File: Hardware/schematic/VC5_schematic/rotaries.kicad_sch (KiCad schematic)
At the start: 39 parts, among them U6 MCP23017

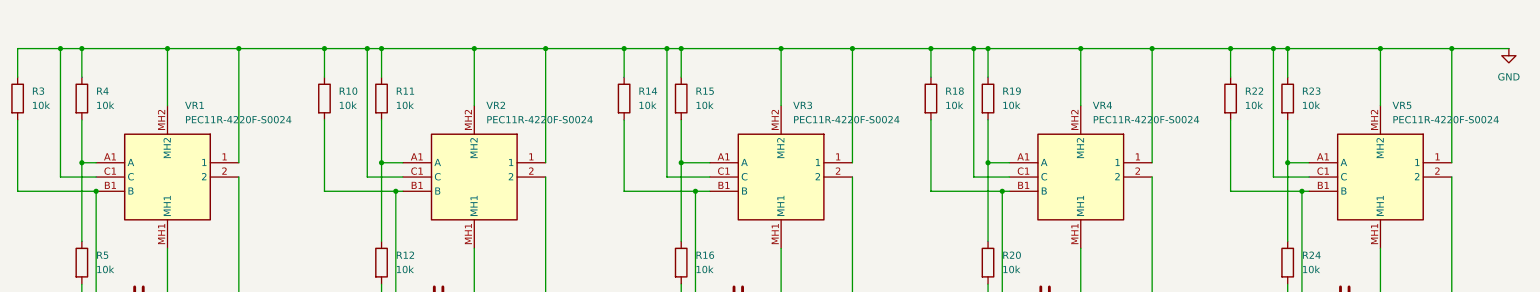
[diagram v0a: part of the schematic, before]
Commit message: fixed an error in the filters for the rotaries
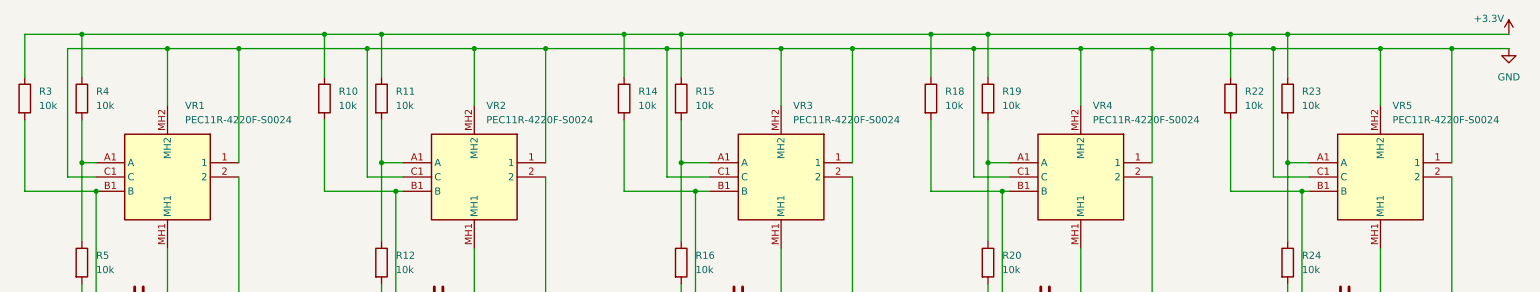
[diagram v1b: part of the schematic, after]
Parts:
- C10, C11, C12, C13, C14, C15, C6, C7, C8, C9: footprint (none) -> Capacitor_THT:C_Disc_D3.8mm_W2.6mm_P2.50mm
- R10, R11, R12, R13, R14, R15, R16, R17, R18, R19, R20, R21, R22, R23, R24, R25, R3, R4, R5, R6: footprint (none) -> Resistor_THT:R_Axial_DIN0204_L3.6mm_D1.6mm_P7.62mm_Horizontal
- R7, R8, R9: footprint Resistor_THT:R_Axial_DIN0207_L6.3mm_D2.5mm_P10.16mm_Horizontal -> Resistor_THT:R_Axial_DIN0204_L3.6mm_D1.6mm_P7.62mm_Horizontal
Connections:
- net +3.3V: now also R10.1, R11.1, R14.1, R15.1, R18.1, R19.1, R22.1, R23.1, R3.1, R4.1
- net GND: no longer R10.1, R11.1, R14.1, R15.1, R18.1, R19.1, R22.1, R23.1, R3.1, R4.1
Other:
- moved on the sheet: R3

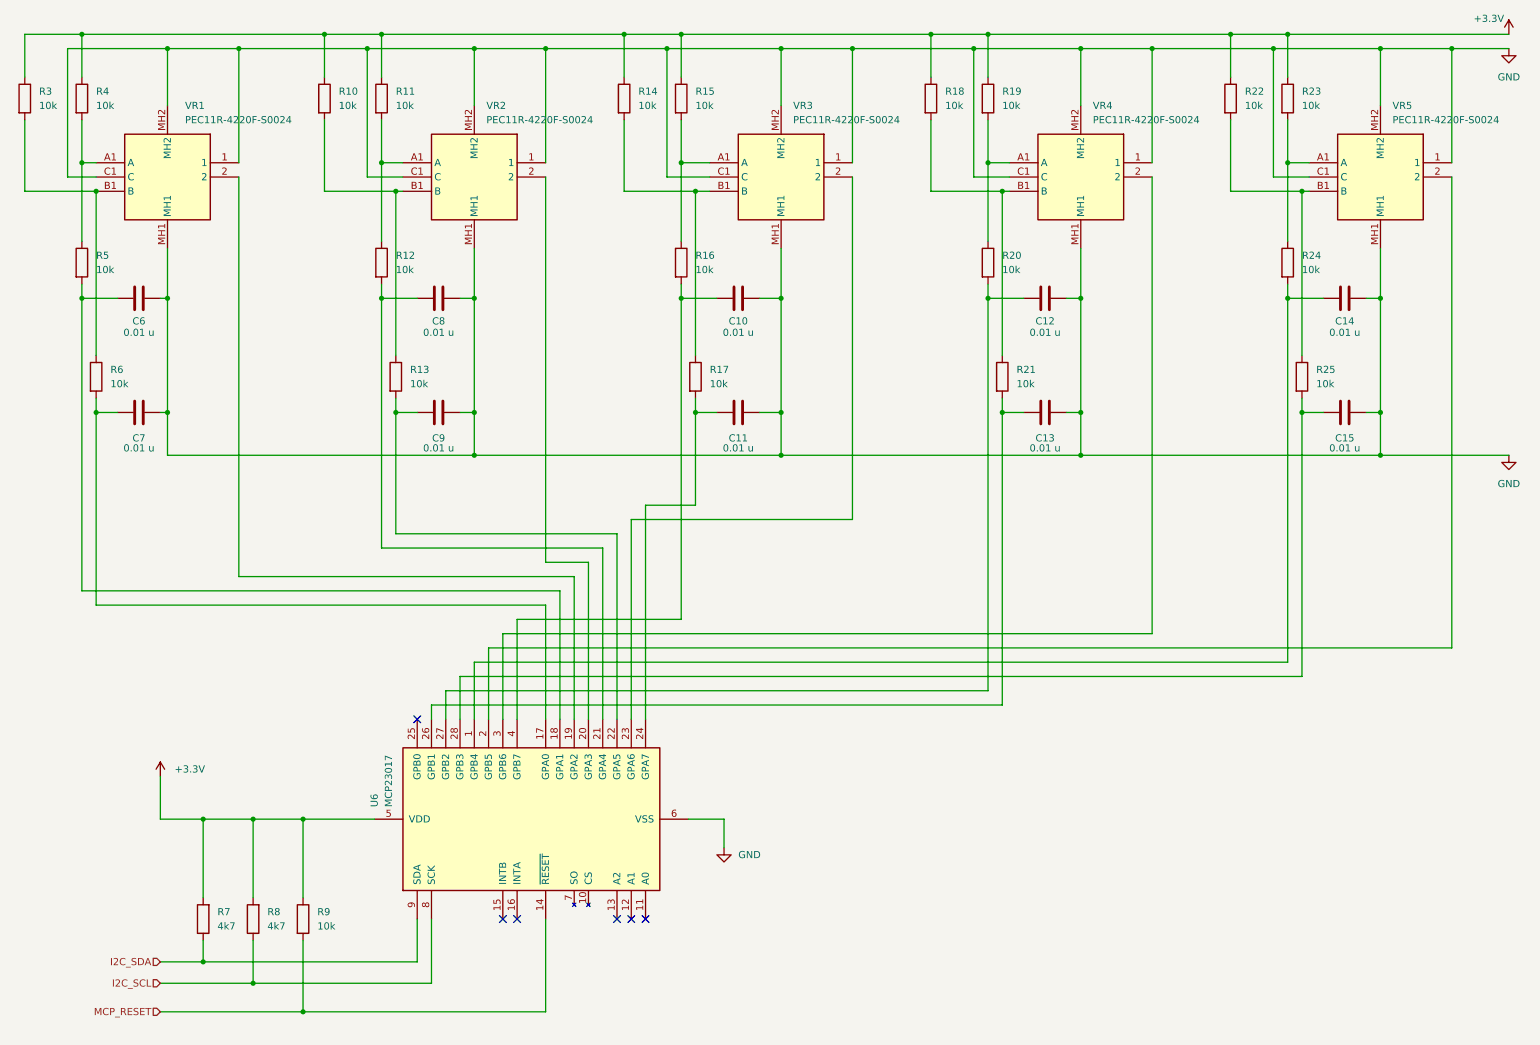
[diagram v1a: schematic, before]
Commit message: updated footprints and corresponding 3D models
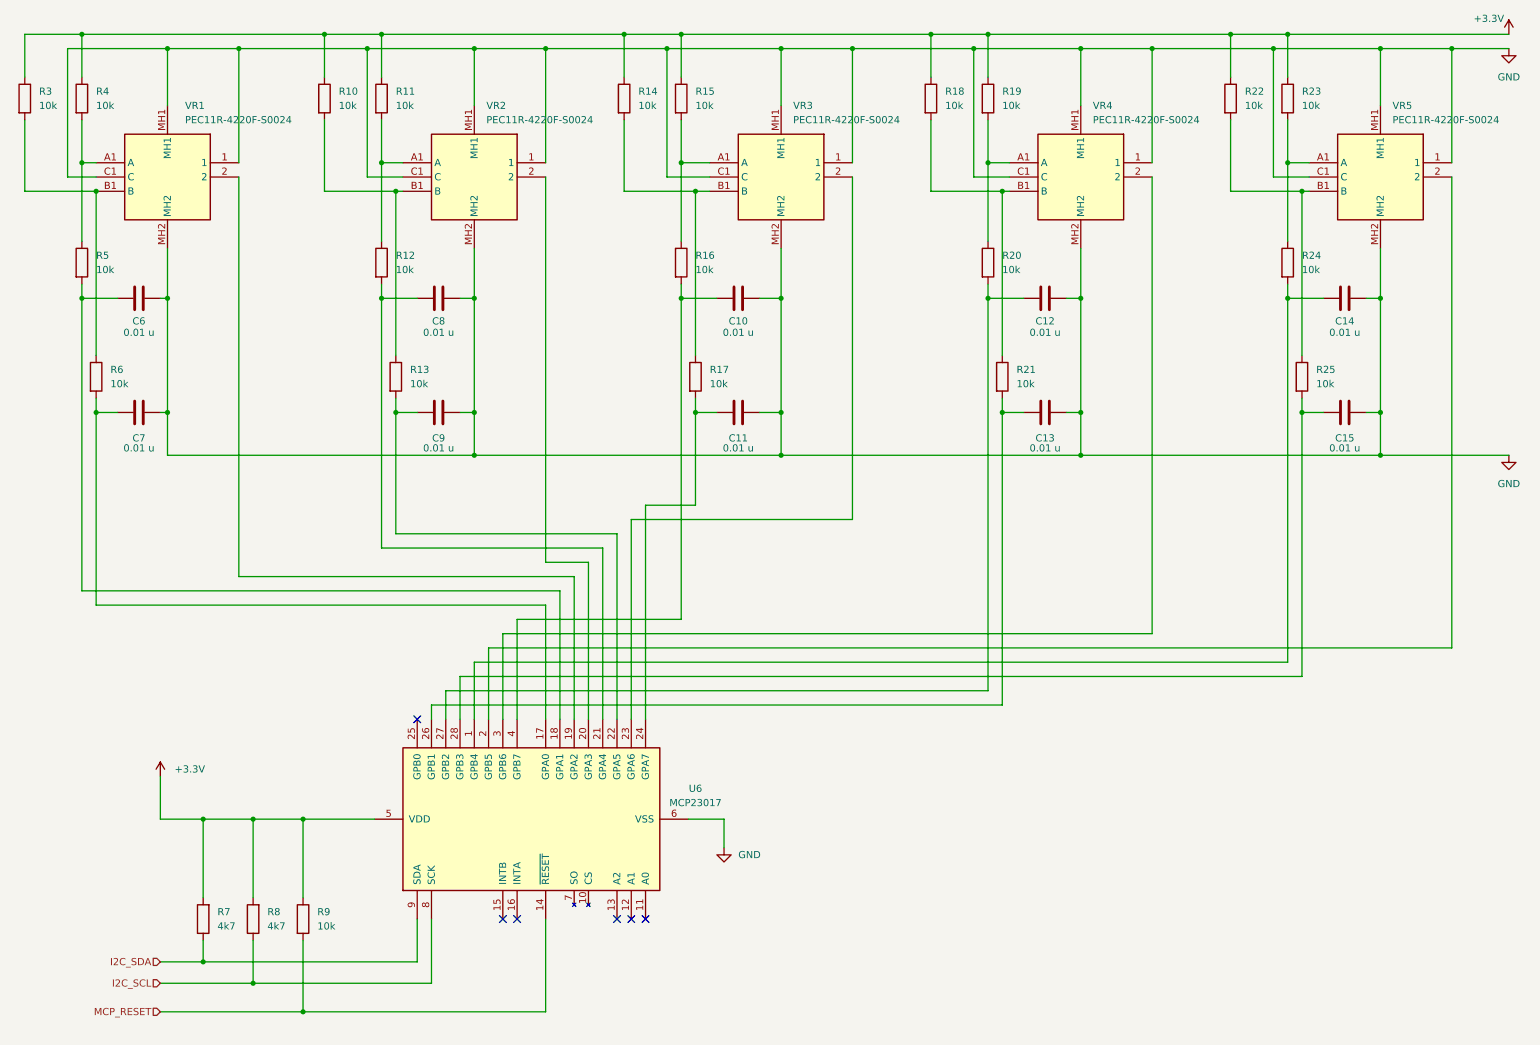
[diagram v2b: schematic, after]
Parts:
- C10, C11, C12, C13, C14, C15, C6, C7, C8, C9: footprint Capacitor_THT:C_Disc_D3.8mm_W2.6mm_P2.50mm -> Capacitor_THT:C_Disc_D5.0mm_W2.5mm_P2.50mm
- VR1, VR2, VR3, VR4, VR5: footprint VC5_footprint_library:PEC11R_4220F_S0024 -> VC5_footprint_library:PEC11R4220FS0024; Arrow Price/Stock https://www.arrow.com/en/products/pec11r-4220f-s0024/bourns?utm_currency=USD&region=nac -> https://www.arrow.com/en/products/pec11r-4220f-s0024/bourns?utm_currency=USD&region=europe
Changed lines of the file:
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@@
 			)
 		)
-		(property "Footprint" "VC5_footprint_library:PEC11R_4220F_S0024"
+		(property "Footprint" "VC5_footprint_library:PEC11R4220FS0024"
 			(at 167.97 50.8 0)
 			(effects
@@
 			)
 		)
-		(property "Arrow Price/Stock" "https://www.arrow.com/en/products/pec11r-4220f-s0024/bourns?utm_currency=USD&region=nac"
+		(property "Arrow Price/Stock" "https://www.arrow.com/en/products/pec11r-4220f-s0024/bourns?utm_currency=USD&region=europe"
 			(at -732.03 50.8 0)
 			(effects
@@
 			)
 		)
-		(property "Footprint" "VC5_footprint_library:PEC11R_4220F_S0024"
+		(property "Footprint" "VC5_footprint_library:PEC11R4220FS0024"
 			(at 114.63 50.8 0)
 			(effects
@@
 			)
 		)
-		(property "Arrow Price/Stock" "https://www.arrow.com/en/products/pec11r-4220f-s0024/bourns?utm_currency=USD&region=nac"
+		(property "Arrow Price/Stock" "https://www.arrow.com/en/products/pec11r-4220f-s0024/bourns?utm_currency=USD&region=europe"
 			(at -785.37 50.8 0)
 			(effects
@@
 	)
 	(symbol
-		(lib_id "VC5_library:MCP23017")
-		(at 106.68 156.21 90)
-		(unit 1)
-		(exclude_from_sim no)
-		(in_bom yes)
-		(on_board yes)
-		(dnp no)
-		(fields_autoplaced yes)
-		(property "Reference" "U6"
-			(at 78.74 154.0667 0)
-			(effects
-				(font
-					(size 1.27 1.27)
-				)
-				(justify left)
-			)
-		)
-		(property "Value" "MCP23017"
-			(at 81.28 154.0667 0)
-			(effects
-				(font
-					(size 1.27 1.27)
-				)
-				(justify left)
-			)
-		)
-		(property "Footprint" "VC5_footprint_library:MCP23017_IO_expander"
-			(at 132.08 151.13 0)
-			(effects
-				(font
-					(size 1.27 1.27)
-				)
-				(justify left)
-				(hide yes)
-			)
-		)
-		(property "Datasheet" "https://www.waveshare.com/wiki/MCP23017_IO_Expansion_Board"
-			(at 134.62 151.13 0)
-			(effects
-				(font
-					(size 1.27 1.27)
-				)
-				(justify left)
-				(hide yes)
-			)
-		)
-		(property "Description" "16-bit I/O expander, I2C, interrupts, w pull-ups, QFN-28"
-			(at 106.68 156.21 0)
-			(effects
-				(font
-					(size 1.27 1.27)
-				)
-				(hide yes)
-			)
-		)
-		(pin "12"
-		)
-		(pin "11"
-		)
-		(pin "6"
-		)
-		(pin "14"
-		)
-		(pin "13"
-		)
-		(pin "16"
-		)
-		(pin "9"
-		)
-		(pin "7"
-		)
-		(pin "5"
-		)
-		(pin "25"
-		)
-		(pin "1"
-		)
-		(pin "8"
-		)
-		(pin "15"
-		)
-		(pin "10"
-		)
-		(pin "26"
-		)
-		(pin "27"
-		)
-		(pin "28"
-		)
-		(pin "2"
-		)
-		(pin "3"
-		)
-		(pin "4"
-		)
-		(pin "17"
-		)
-		(pin "18"
-		)
-		(pin "19"
-		)
-		(pin "20"
-		)
-		(pin "21"
-		)
-		(pin "24"
-		)
-		(pin "23"
-		)
-		(pin "22"
-		)
-		(instances
-			(project ""
-				(path "/5ac87209-2525-401a-b136-a9d04031b521/fc2974f5-8ba8-49d8-a499-cee7d56a2b2e"
-					(reference "U6")
-					(unit 1)
-				)
-			)
-		)
-	)
-	(symbol
 		(lib_id "VC5_library:PEC11R-4220F-S0024")
 		(at 96.52 29.21 270)
@@
 			)
 		)
-		(property "Footprint" "VC5_footprint_library:PEC11R_4220F_S0024"
+		(property "Footprint" "VC5_footprint_library:PEC11R4220FS0024"
 			(at 6.68 50.8 0)
 			(effects
@@
 			)
 		)
-		(property "Arrow Price/Stock" "https://www.arrow.com/en/products/pec11r-4220f-s0024/bourns?utm_currency=USD&region=nac"
+		(property "Arrow Price/Stock" "https://www.arrow.com/en/products/pec11r-4220f-s0024/bourns?utm_currency=USD&region=europe"
 			(at -893.32 50.8 0)
 			(effects
@@
 			)
 		)
-		(property "Footprint" "VC5_footprint_library:PEC11R_4220F_S0024"
+		(property "Footprint" "VC5_footprint_library:PEC11R4220FS0024"
 			(at 61.29 50.8 0)
 			(effects
@@
 			)
 		)
-		(property "Arrow Price/Stock" "https://www.arrow.com/en/products/pec11r-4220f-s0024/bourns?utm_currency=USD&region=nac"
+		(property "Arrow Price/Stock" "https://www.arrow.com/en/products/pec11r-4220f-s0024/bourns?utm_currency=USD&region=europe"
 			(at -838.71 50.8 0)
 			(effects
@@
 			)
 		)
-		(property "Footprint" "Capacitor_THT:C_Disc_D3.8mm_W2.6mm_P2.50mm"
+		(property "Footprint" "Capacitor_THT:C_Disc_D5.0mm_W2.5mm_P2.50mm"
 			(at 255.27 62.5348 0)
 			(effects
@@
 			)
 		)
-		(property "Footprint" "Capacitor_THT:C_Disc_D3.8mm_W2.6mm_P2.50mm"
+		(property "Footprint" "Capacitor_THT:C_Disc_D5.0mm_W2.5mm_P2.50mm"
 			(at 147.32 82.8548 0)
 			(effects
@@
 			)
 		)
-		(property "Footprint" "Capacitor_THT:C_Disc_D3.8mm_W2.6mm_P2.50mm"
+		(property "Footprint" "Capacitor_THT:C_Disc_D5.0mm_W2.5mm_P2.50mm"
 			(at 93.98 62.5348 0)
 			(effects
@@
 			)
 		)
-		(property "Footprint" "Capacitor_THT:C_Disc_D3.8mm_W2.6mm_P2.50mm"
+		(property "Footprint" "Capacitor_THT:C_Disc_D5.0mm_W2.5mm_P2.50mm"
 			(at 40.64 62.5348 0)
 			(effects
@@
 			)
 		)
-		(property "Footprint" "Capacitor_THT:C_Disc_D3.8mm_W2.6mm_P2.50mm"
+		(property "Footprint" "Capacitor_THT:C_Disc_D5.0mm_W2.5mm_P2.50mm"
 			(at 93.98 82.8548 0)
 			(effects
@@
 			)
 		)
-		(property "Footprint" "Capacitor_THT:C_Disc_D3.8mm_W2.6mm_P2.50mm"
+		(property "Footprint" "Capacitor_THT:C_Disc_D5.0mm_W2.5mm_P2.50mm"
 			(at 255.27 82.8548 0)
 			(effects
@@
 			)
 		)
-		(property "Footprint" "Capacitor_THT:C_Disc_D3.8mm_W2.6mm_P2.50mm"
+		(property "Footprint" "Capacitor_THT:C_Disc_D5.0mm_W2.5mm_P2.50mm"
 			(at 201.93 82.8548 0)
 			(effects
@@
 			)
 		)
-		(property "Footprint" "Capacitor_THT:C_Disc_D3.8mm_W2.6mm_P2.50mm"
+		(property "Footprint" "Capacitor_THT:C_Disc_D5.0mm_W2.5mm_P2.50mm"
 			(at 40.64 82.8548 0)
 			(effects
@@
 			)
 		)
-		(property "Footprint" "VC5_footprint_library:PEC11R_4220F_S0024"
+		(property "Footprint" "VC5_footprint_library:PEC11R4220FS0024"
 			(at -47.93 50.8 0)
 			(effects
@@
 			)
 		)
-		(property "Arrow Price/Stock" "https://www.arrow.com/en/products/pec11r-4220f-s0024/bourns?utm_currency=USD&region=nac"
+		(property "Arrow Price/Stock" "https://www.arrow.com/en/products/pec11r-4220f-s0024/bourns?utm_currency=USD&region=europe"
 			(at -947.93 50.8 0)
 			(effects
@@
 			)
 		)
-		(property "Footprint" "Capacitor_THT:C_Disc_D3.8mm_W2.6mm_P2.50mm"
+		(property "Footprint" "Capacitor_THT:C_Disc_D5.0mm_W2.5mm_P2.50mm"
 			(at 201.93 62.5348 0)
 			(effects
@@
 			)
 		)
-		(property "Footprint" "Capacitor_THT:C_Disc_D3.8mm_W2.6mm_P2.50mm"
+		(property "Footprint" "Capacitor_THT:C_Disc_D5.0mm_W2.5mm_P2.50mm"
 			(at 147.32 62.5348 0)
 			(effects
@@
 					(unit 1)
 				)
+			)
+		)
+	)
+	(symbol
+		(lib_id "VC5_library:MCP23017")
+		(at 106.68 156.21 90)
+		(unit 1)
+		(exclude_from_sim no)
+		(in_bom yes)
+		(on_board yes)
+		(dnp no)
+		(fields_autoplaced yes)
+		(property "Reference" "U6"
+			(at 135.89 150.7646 90)
+			(effects
+				(font
+					(size 1.27 1.27)
+				)
+			)
+		)
+		(property "Value" "MCP23017"
+			(at 135.89 153.3046 90)
+			(effects
+				(font
+					(size 1.27 1.27)
+				)
+			)
+		)
+		(property "Footprint" "VC5_footprint_library:MCP23017_IO_expander"
+			(at 132.08 151.13 0)
+			(effects
+				(font
+					(size 1.27 1.27)
+				)
+				(justify left)
+				(hide yes)
+			)
+		)
+		(property "Datasheet" "https://www.waveshare.com/wiki/MCP23017_IO_Expansion_Board"
+			(at 134.62 151.13 0)
+			(effects
+				(font
+					(size 1.27 1.27)
+				)
+				(justify left)
+				(hide yes)
+			)
+		)
+		(property "Description" "16-bit I/O expander, I2C, interrupts, w pull-ups, QFN-28"
+			(at 106.68 156.21 0)
+			(effects
+				(font
+					(size 1.27 1.27)
+				)
+				(hide yes)
+			)
+		)
+		(pin "13"
+		)
+		(pin "27"
+		)
+		(pin "12"
+		)
+		(pin "8"
+		)
+		(pin "11"
+		)
+		(pin "9"
+		)
+		(pin "16"
+		)
+		(pin "25"
+		)
+		(pin "26"
+		)
+		(pin "6"
+		)
+		(pin "15"
+		)
+		(pin "14"
+		)
+		(pin "7"
+		)
+		(pin "10"
+		)
+		(pin "5"
+		)
+		(pin "23"
+		)
+		(pin "22"
+		)
+		(pin "20"
+		)
+		(pin "19"
+		)
+		(pin "28"
+		)
+		(pin "3"
+		)
+		(pin "18"
+		)
+		(pin "2"
+		)
+		(pin "1"
+		)
+		(pin "4"
+		)
+		(pin "21"
+		)
+		(pin "17"
+		)
+		(pin "24"
+		)
+		(instances
+			(project ""
+				(path "/5ac87209-2525-401a-b136-a9d04031b521/fc2974f5-8ba8-49d8-a499-cee7d56a2b2e"
+					(reference "U6")
+					(unit 1)
+				)

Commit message: trace routing completed
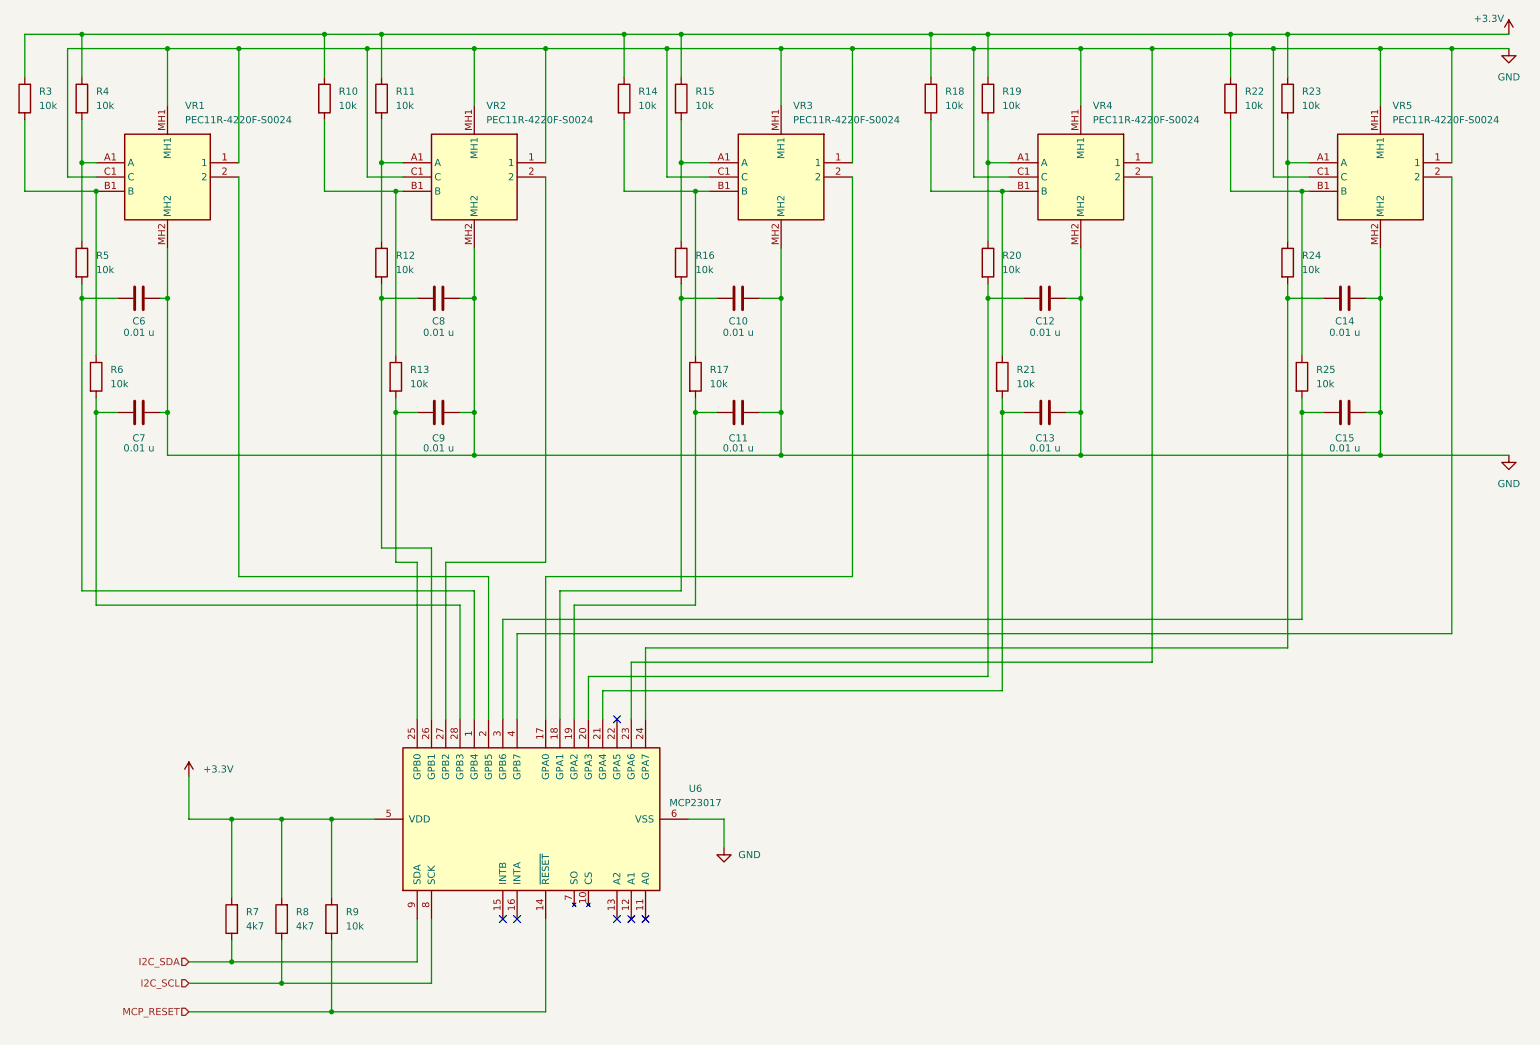
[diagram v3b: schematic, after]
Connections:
- net at VR5.2: now also U6.4 (GPB7); no longer U6.2 (GPB5)
- net at C9.1, R13.2: now also U6.25 (GPB0); no longer U6.22 (GPA5)
- net at VR4.2: now also U6.23 (GPA6); no longer U6.3 (GPB6)
- net at VR2.2: now also U6.27 (GPB2); no longer U6.20 (GPA3)
- net at VR3.2: now also U6.17 (GPA0); no longer U6.23 (GPA6)
- net at C14.1, R24.2: now also U6.24 (GPA7); no longer U6.1 (GPB4)
- net at C13.1, R21.2: now also U6.21 (GPA4); no longer U6.26 (GPB1)
- net at C7.1, R6.2: now also U6.28 (GPB3); no longer U6.17 (GPA0)
- net at C11.1, R17.2: now also U6.19 (GPA2); no longer U6.24 (GPA7)
- net at C8.1, R12.2: now also U6.26 (GPB1); no longer U6.21 (GPA4)
- net at C6.1, R5.2: now also U6.1 (GPB4); no longer U6.18 (GPA1)
- net at C15.1, R25.2: now also U6.3 (GPB6); no longer U6.28 (GPB3)
- net at C10.1, R16.2: now also U6.18 (GPA1); no longer U6.4 (GPB7)
- net at VR1.2: now also U6.2 (GPB5); no longer U6.19 (GPA2)
- net at C12.1, R20.2: now also U6.20 (GPA3); no longer U6.27 (GPB2)
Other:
- moved on the sheet: R7, R8, R9
